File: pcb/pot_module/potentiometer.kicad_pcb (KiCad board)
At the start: 2 copper layers, 75.5 x 20 mm, 6 parts, among them J1 Conn_01x03

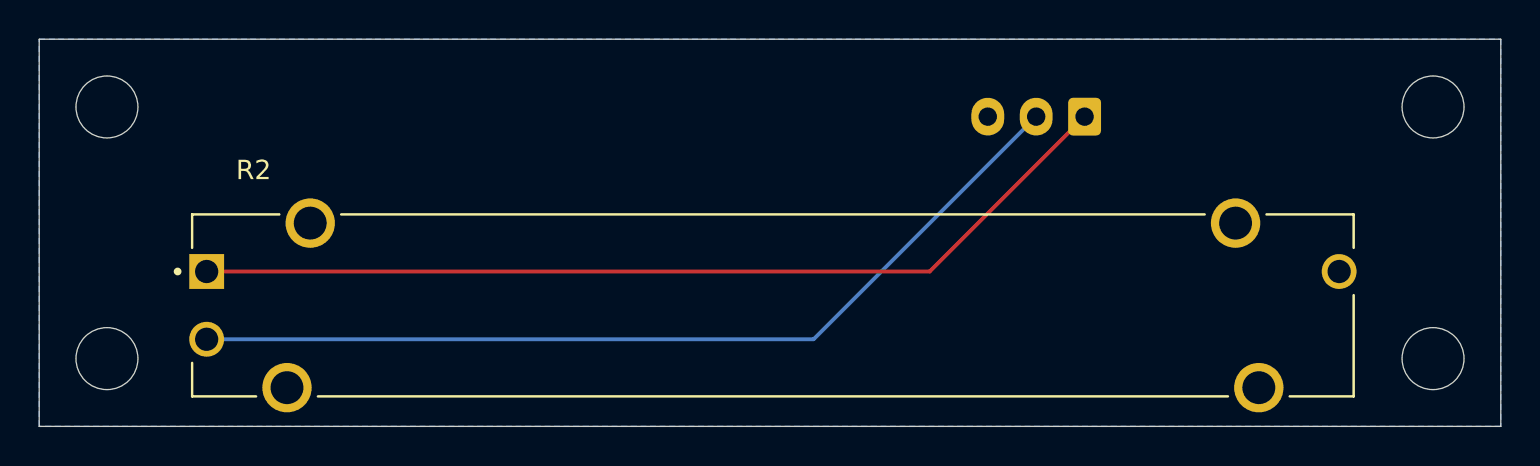
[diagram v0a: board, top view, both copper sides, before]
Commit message: Tweak pot module
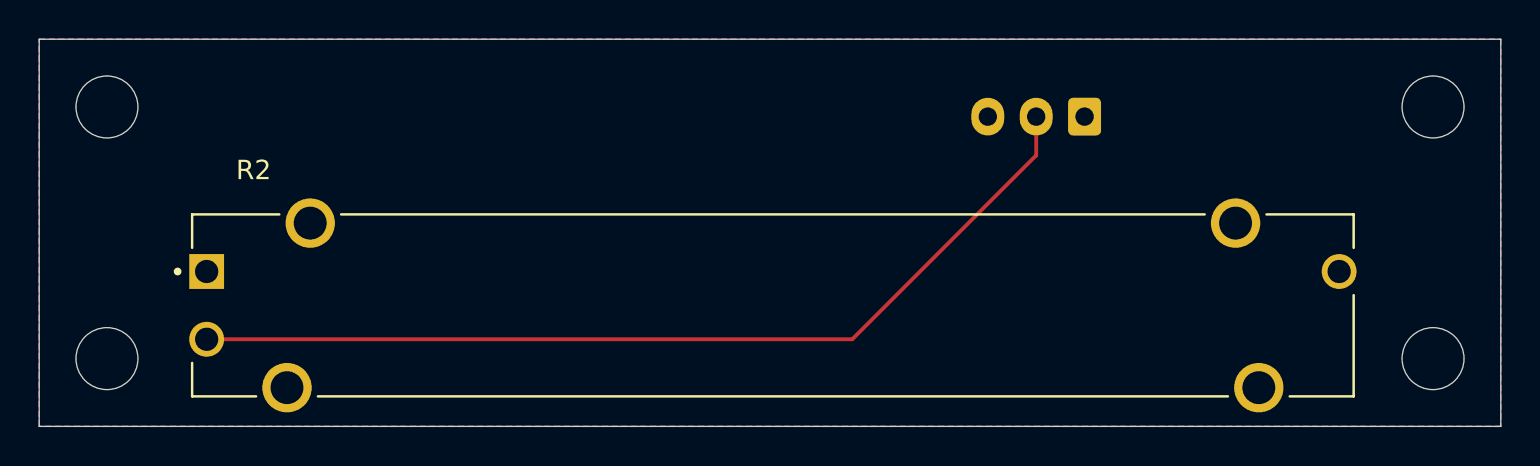
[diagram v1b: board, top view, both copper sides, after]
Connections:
- net Net-(J1-Pin_1) renamed Plane2
- net Plane renamed Plane1
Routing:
- net Plane2: track 48.7 -> 0.00 mm
- net Net-(J1-Pin_2): track 47.6 -> 48.8 mm
- added copper zone on F.Cu, net Plane1
- added copper zone on B.Cu, net Plane2
- removed copper zone on B.Cu, net Plane1
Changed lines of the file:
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@@
 			(layers "*.Cu" "*.Mask")
 			(remove_unused_layers no)
-			(net "Net-(J1-Pin_1)")
+			(net "Plane2")
 			(pintype "passive")
 			(solder_mask_margin 0.102)
@@
 			(layers "*.Cu" "*.Mask")
 			(remove_unused_layers no)
-			(net "Plane")
+			(net "Plane1")
 			(pintype "passive")
 			(solder_mask_margin 0.102)
@@
 			(layers "*.Cu" "*.Mask")
 			(remove_unused_layers no)
-			(net "Plane")
+			(net "Plane1")
 			(pinfunction "SHIELD_SH1")
 			(pintype "passive")
@@
 			(layers "*.Cu" "*.Mask")
 			(remove_unused_layers no)
-			(net "Plane")
+			(net "Plane1")
 			(pinfunction "SHIELD__1_SH2")
 			(pintype "passive")
@@
 			(layers "*.Cu" "*.Mask")
 			(remove_unused_layers no)
-			(net "Plane")
+			(net "Plane1")
 			(pinfunction "SHIELD__2_SH3")
 			(pintype "passive")
@@
 			(layers "*.Cu" "*.Mask")
 			(remove_unused_layers no)
-			(net "Plane")
+			(net "Plane1")
 			(pinfunction "SHIELD__3_SH4")
 			(pintype "passive")
@@
 		(tags "connector JST XA vertical")
 		(property "Reference" "J1"
-			(at 2.5 4.4 0)
+			(at 9.5 2.5 0)
 			(layer "B.SilkS")
 			(effects
@@
 			(remove_unused_layers no)
 			(roundrect_rratio 0.147059)
-			(net "Net-(J1-Pin_1)")
+			(net "Plane2")
 			(pinfunction "Pin_1_1")
 			(pintype "passive")
@@
 			(layers "*.Cu" "*.Mask")
 			(remove_unused_layers no)
-			(net "Plane")
+			(net "Plane1")
 			(pinfunction "Pin_3_3")
 			(pintype "passive")
@@
 	)
 	(segment
-		(start 142 81)
-		(end 150 73)
+		(start 147.5 73)
+		(end 147.5 75)
 		(width 0.2)
 		(layer "F.Cu")
-		(net "Net-(J1-Pin_1)")
+		(net "Net-(J1-Pin_2)")
 	)
 	(segment
-		(start 104.65 81)
-		(end 142 81)
+		(start 138 84.5)
+		(end 104.65 84.5)
 		(width 0.2)
 		(layer "F.Cu")
-		(net "Net-(J1-Pin_1)")
+		(net "Net-(J1-Pin_2)")
 	)
 	(segment
-		(start 136 84.5)
-		(end 147.5 73)
+		(start 147.5 75)
+		(end 138 84.5)
 		(width 0.2)
-		(layer "B.Cu")
+		(layer "F.Cu")
 		(net "Net-(J1-Pin_2)")
 	)
-	(segment
-		(start 104.65 84.5)
-		(end 136 84.5)
-		(width 0.2)
-		(layer "B.Cu")
-		(net "Net-(J1-Pin_2)")
-	)
 	(zone
-		(net "Plane")
+		(net "Plane1")
+		(layer "F.Cu")
+		(hatch edge 0.5)
+		(priority 1)
+		(connect_pads
+			(clearance 0.5)
+		)
+		(min_thickness 0.25)
+		(fill yes
+			(thermal_gap 0.5)
+			(thermal_bridge_width 0.5)
+			(island_removal_mode 0)
+		)
+		(polygon
+			(pts
+				(xy 171.5 69) (xy 171.5 89) (xy 96 89) (xy 96 69)
+			)
+		)
+	)
+	(zone
+		(net "Plane2")
 		(layer "B.Cu")
 		(hatch edge 0.5)
